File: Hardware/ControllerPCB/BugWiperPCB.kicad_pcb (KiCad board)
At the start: 4 copper layers, 110 x 40 mm, 115 parts, among them J1 UJ20-C-H-G-SMT-1-P16-TR, J2 1770924, J3 Phoenix_1776508, J4 RJ45, J5 Conn_TagConnect_TC2030-NL_ESP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, J6 1824420000, J7 Conn_01x02_Pin, J8 Micro_SD_Card, Q1 SQJ146ELP-T1_GE3, U1 ESP32-S3-WROOM-1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

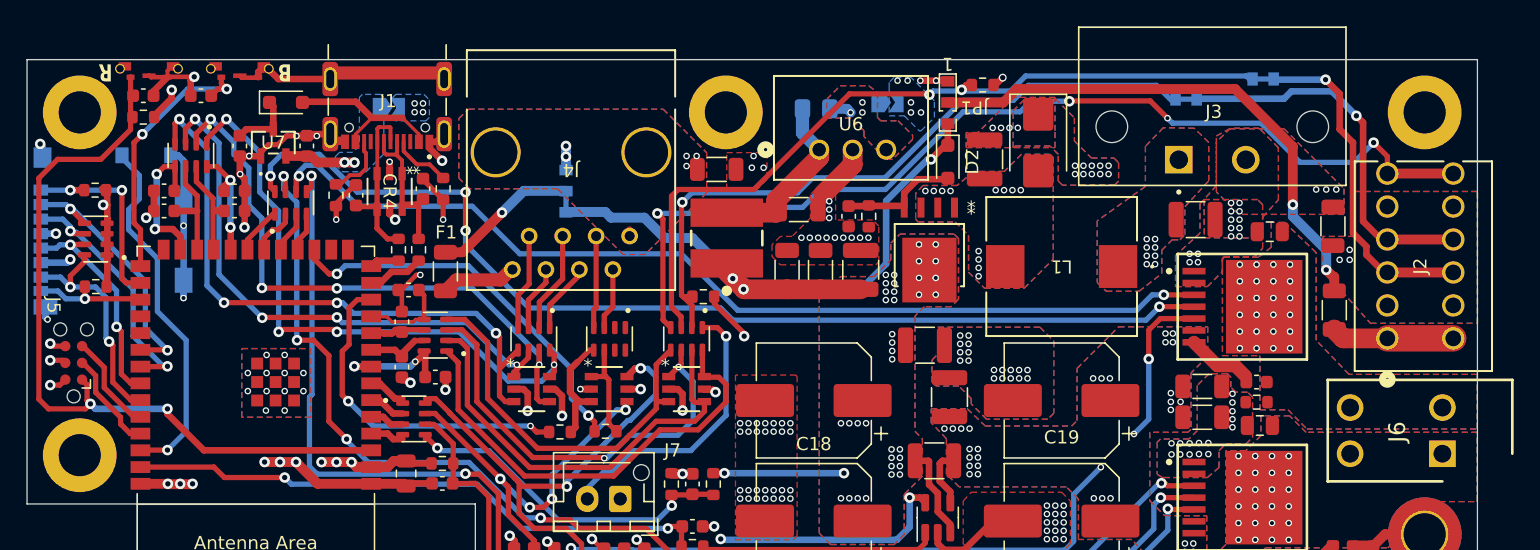
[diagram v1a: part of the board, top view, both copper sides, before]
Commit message: update PCB and Gerber
change Switches to cheaper ones
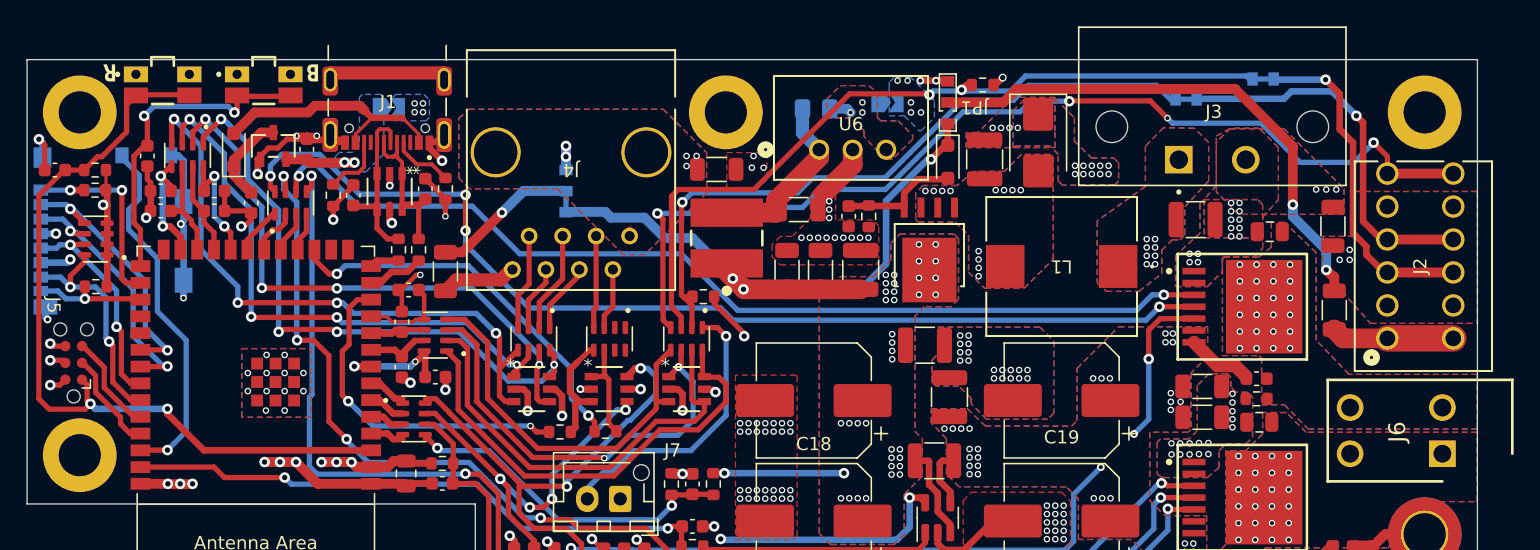
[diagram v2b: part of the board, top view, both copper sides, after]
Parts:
- removed S1, S2: EVP-AT2L1B000, BugWiper_lib:SW_EVP-AT2L1B000
- added SW1: SW_Push, BugWiper_lib:EVQ9P701P, F.Cu at (128.0, 60.5)
- added SW2: SW_Push, BugWiper_lib:EVQ9P701P, F.Cu at (120.3, 60.5)
- C18, C19, C20, C28: value 470uF 16V -> 330uF 25V
- D2: value D_Zener 10V -> GDZ10B-E3-08
- F1, F2, F3, F4: value 100mA Polyfuse -> PTS120630V012
- J3: value Phoenix_1776508 -> 1776508
- J4: value RJ45 -> 54602-908LF
- J7: value Conn_01x02_Pin -> B2B-XH-AM(LF)(SN)
- J8: value Micro_SD_Card -> 104031-0811
- L1: value IHLP4040DZER100M1A -> IHLP4040DZER100M11
- L2: value 10µH 2.2A -> 10uH 2.2A 74477410
- TH1: value Thermistor_NTC -> 10k NTC
- moved C4 8.76 mm to (112.1, 68.4), turned to 180 degrees
- moved C3 6.12 mm to (119.1, 67.3), turned to -90 degrees
- moved R6 5.43 mm to (115.2, 68.4)
- moved D1 5.36 mm to (125.7, 66.9), turned to 90 degrees
- moved C30 4.40 mm to (127.0, 70.9)
- moved C32 1.52 mm to (124.2, 70.0)
- moved C33 1.52 mm to (124.2, 71.5)
- moved C29 0.25 mm to (131.2, 66.8)
- moved C34 0.25 mm to (120.1, 71.5)
- moved C35 0.25 mm to (120.1, 70.0)
- moved C8 0.25 mm to (203.2, 84.2)
- moved R8 0.25 mm to (203.2, 85.7)
- moved U7 0.25 mm to (128.7, 66.5)
- moved RN4 0.25 mm to (122.2, 67.3)
- moved C5 0.25 mm to (203.5, 87.5)
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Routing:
- net GND: track 133.3 -> 122.6 mm, vias 173 -> 171
- net Net-(D1-A): track 12.3 -> 18.3 mm
- net Boot: track 44.1 -> 49.1 mm
- net EN: track 58.7 -> 60.7 mm
- net +5V: track 5.05 -> 6.89 mm
- net IN_4: track 10.9 -> 9.11 mm
- net +3.3V: track 50.0 -> 49.1 mm, vias 26 -> 25
- net IN_1: track 8.51 -> 9.39 mm
- net IN_2: track 7.65 -> 6.96 mm
- net Net-(CR1-IO_1): track 43.6 -> 44.1 mm

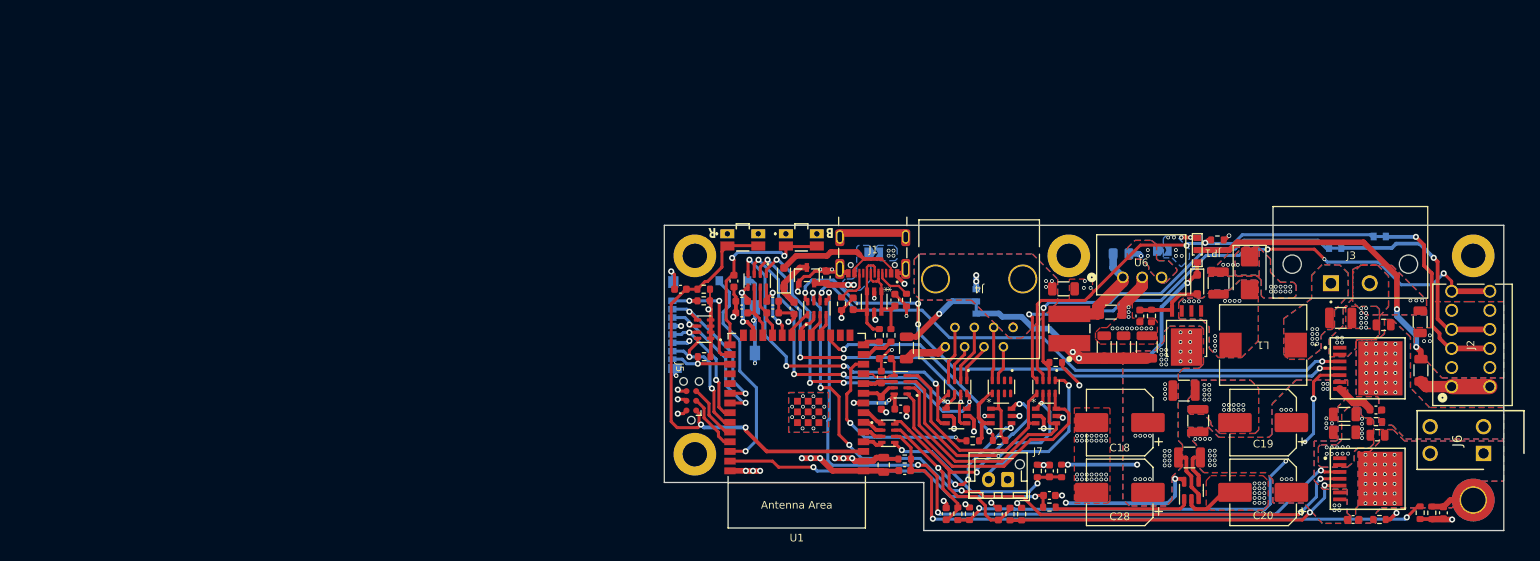
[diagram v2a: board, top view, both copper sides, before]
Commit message: update PCB to view Values and Refs
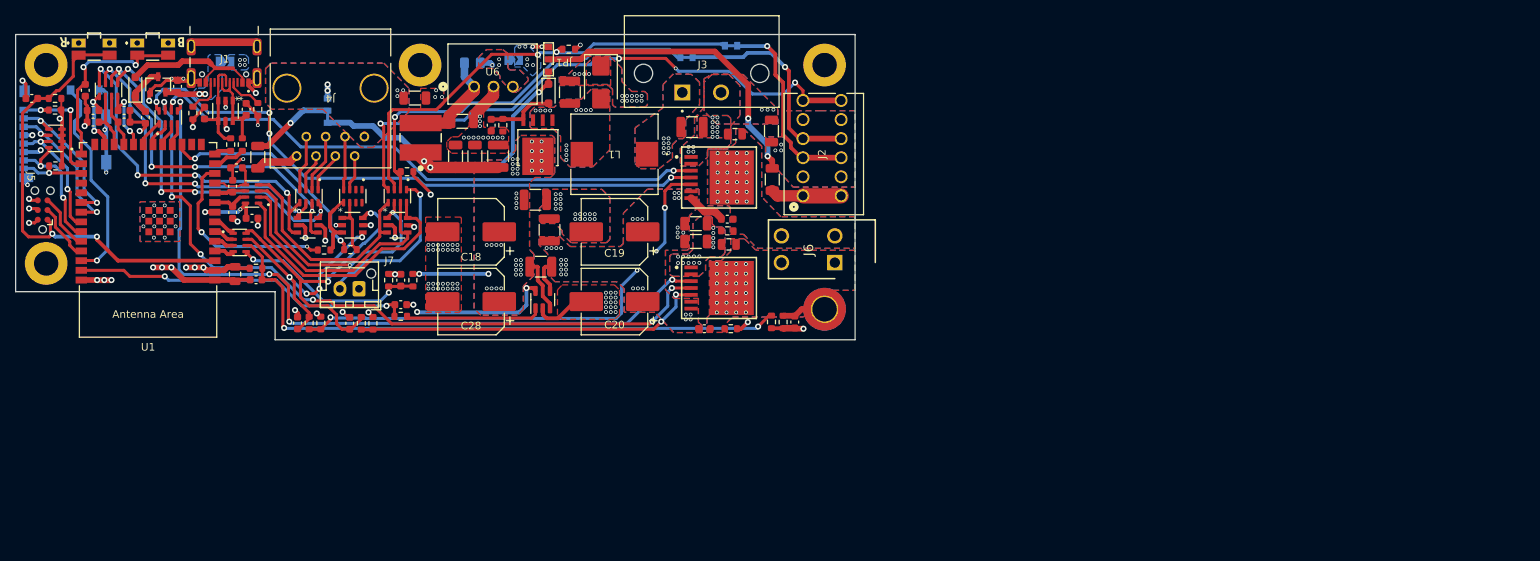
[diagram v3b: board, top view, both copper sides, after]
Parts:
- C1, C11, C12, C13, C2, C6, C8: footprint Capacitor_SMD:C_0603_1608Metric -> BugWiper_lib:C_0603_1608Metric
- C10, C15, C16, C17, C21, C23, C24, C25, C26, C7: value 22uF 25V -> 22uF
- C14, C32, C33, C34, C35, C36, C37: value 10nF -> 10nF; footprint Capacitor_SMD:C_0603_1608Metric -> BugWiper_lib:C_0603_1608Metric
- C18, C19, C20, C28: value 330uF 25V -> 330uF
- C22, C27, C29, C3, C30, C31, C38, C39, C4: value 100nF -> 100nF; footprint Capacitor_SMD:C_0603_1608Metric -> BugWiper_lib:C_0603_1608Metric
- C40, C5, C9: value 1uF 50V -> 1uF
- CR4: value D5V0P4UR6SO-7 -> D5V0P4UR6
- D2: value GDZ10B-E3-08 -> GDZ10B
- D3: value D_TVS 15V -> D_TVS 14V
- Q1: value SQJ146ELP-T1_GE3 -> SQJ146EL
- R10, R11, R12, R13, R14, R15, R16, R17, R18, R19, R2, R20, R21, R22, R27, R3, R38, R4, R5, R6, R9, TH1: footprint Resistor_SMD:R_0603_1608Metric -> BugWiper_lib:R_0603_1608Metric
- R7, R8: value 47k -> 22k; footprint Resistor_SMD:R_0603_1608Metric -> BugWiper_lib:R_0603_1608Metric
- RN1, RN2, RN5: value 1k x 4 -> 4x1k
- RN3, RN6, RN7: value 100R x 4 -> 4x100R
- RN4, RN8: value 10k x 4 -> 4x10k
- U7: value AP7333-33SRG-7 -> AP7333
- moved C14 88.6 mm to (87.3, 46.9)
- moved C16 88.6 mm to (93.1, 56.7)
- moved C17 88.6 mm to (88.2, 50.9)
- moved C5 88.6 mm to (118.5, 62.5)
- moved CR2 88.6 mm to (75.0, 60.0)
- moved F4 88.6 mm to (77.3, 43.3)
- moved J7 88.6 mm to (70.0, 68.3)
- moved JP2 88.6 mm to (112.1, 38.0)
- moved L2 88.6 mm to (78.1, 48.5)
- moved R10 88.6 mm to (70.3, 72.8)
- moved R19 88.6 mm to (73.9, 67.2)
- moved R21 88.6 mm to (88.8, 46.9)
- moved R3 88.6 mm to (48.2, 45.3)
- moved R9 88.6 mm to (71.8, 72.8)
- moved RN7 88.6 mm to (75.0, 56.2)
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
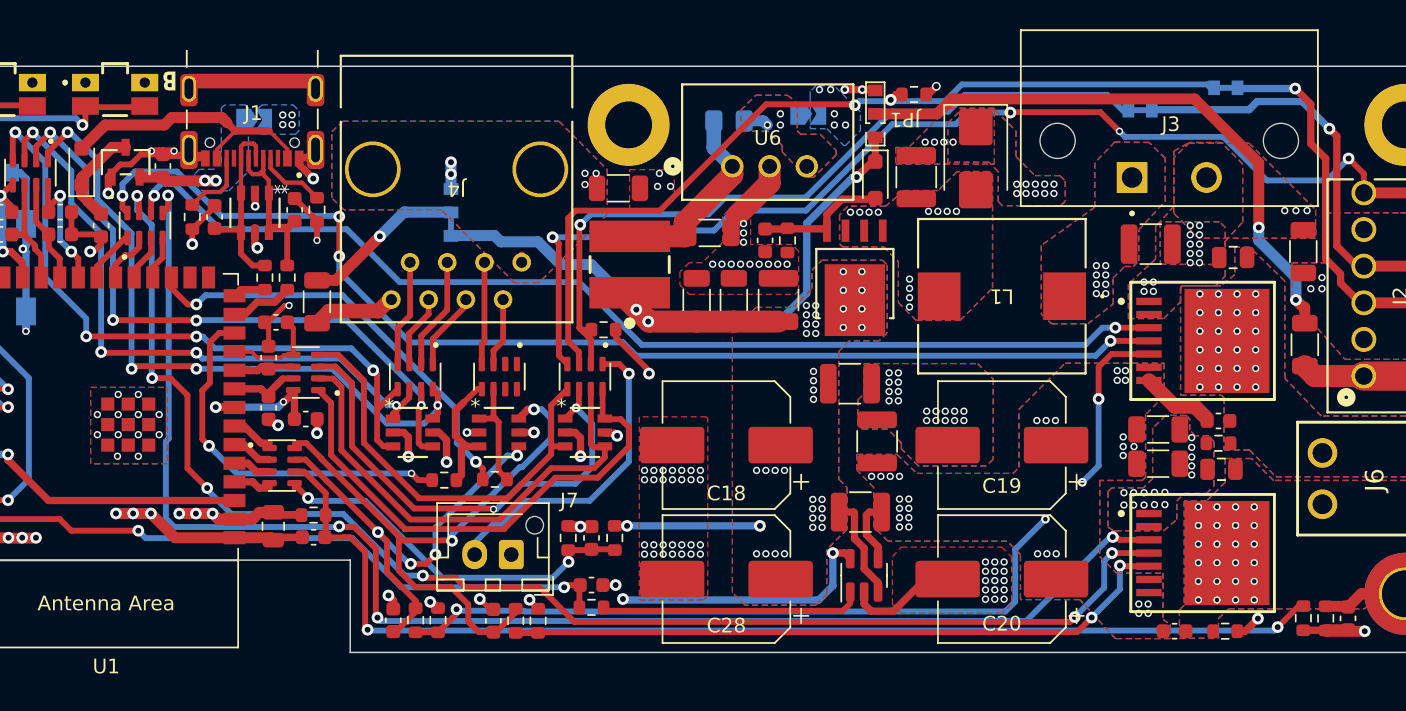
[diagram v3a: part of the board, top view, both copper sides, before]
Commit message: update Controller PCB PDF Export and layer of Values and Reference
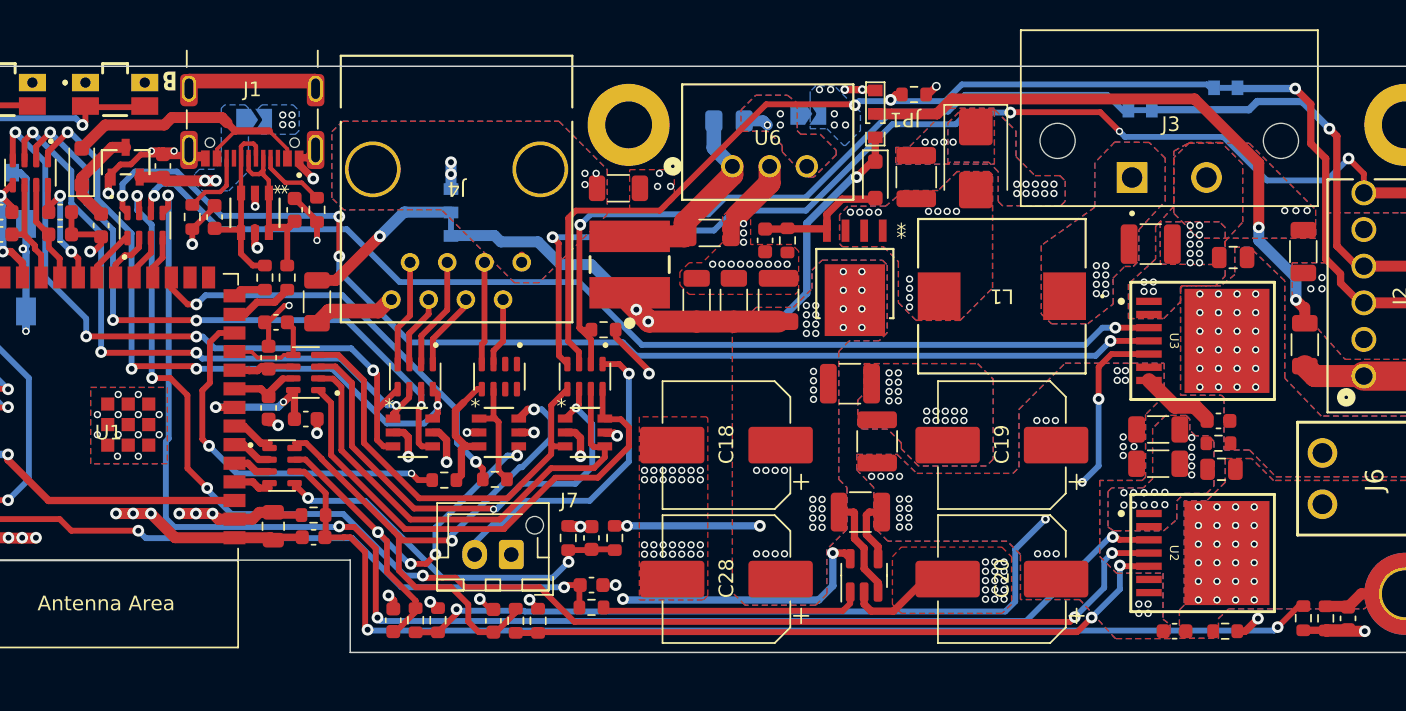
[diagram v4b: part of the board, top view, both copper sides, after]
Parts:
- C10, C24, C25, C26, C7: footprint Capacitor_SMD:C_1206_3216Metric -> BugWiper_lib:C_1206_3216Metric
- C15, C16, C17, C21, C23: footprint Capacitor_SMD:C_1210_3225Metric -> BugWiper_lib:C_1210_3225Metric
- C18, C19, C20, C28: footprint Capacitor_SMD:CP_Elec_8x10.5 -> BugWiper_lib:CP_Elec_8x10.5
- C40, C5, C9: footprint Capacitor_SMD:C_0805_2012Metric -> BugWiper_lib:C_0805_2012Metric
- CR1, CR2, CR3: value D5V0P4UR6SO-7 -> D5V0P4UR6
- D1, D2: footprint Diode_SMD:D_SOD-323_HandSoldering -> BugWiper_lib:D_SOD-323_HandSoldering
- D3: footprint Diode_SMD:D_SMB -> BugWiper_lib:D_SMB
- F1, F2, F3, F4: footprint Resistor_SMD:R_1206_3216Metric -> BugWiper_lib:R_1206_3216Metric
- Q1: value SQJ146EL -> SQJ146ELP
- R25: footprint Resistor_SMD:R_1210_3225Metric -> BugWiper_lib:R_1210_3225Metric
- U4: footprint Package_TO_SOT_SMD:SOT-23-5 -> BugWiper_lib:SOT-23-5
- U7: value AP7333 -> AP7333-33SRG-7
